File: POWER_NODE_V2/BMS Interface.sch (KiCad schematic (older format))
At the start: 0 parts

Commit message: WIP
making good progress
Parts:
- added J?: CONN_02X07, symbol CONN_02X07
- added J?: CONN_01X02, symbol CONN_01X02
- added Q?: Q_NMOS_GSD, symbol Q_NMOS_GSD
- added R? (x2): 10K / .1W / 1% / SMD 0603, symbol R
- added R?: 100 / .1W / 10% / SMD 0603, symbol R
- added U?: MAX14850AEE+, symbol MAX14850AEE+
- added U?: MAX14932, symbol MAX14932
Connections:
- net BMS_ALERT: now also U?.5 (OUTA2)
- net BMS_COMMS_EN: now also J?.13 (P13)
- net BMS_CONV: now also U?.3 (INA1)
- net BMS_DRDY: now also U?.5 (OUTA2)
- net BMS_FAN: now also R?.2
- net BMS_FAULT: now also U?.4 (OUTA1)
- net BMS_MISO: now also U?.4 (OUTA1)
- net BMS_MOSI: now also U?.2 (INA1)
- net BMS_NCS: now also R?.2, U?.6 (IOA1)
- net BMS_SCK: now also U?.3 (INA2)
- new net: J?.7 (P7), U?.11 (IOB1)
- new net: J?.4 (P4), R?.2, U?.12 (INB2)
- new net: J?.1 (P1), U?.13 (INB1)
- new net: J?.5 (P5), U?.14 (OUTB2)
- new net: J?.3 (P3), U?.15 (OUTB1)
- new net: J?.14 (P14), R?.1, U?.16 (VCCB), U?.16 (VCCB)
- new net: J?.2 (P2), U?.15 (GNDB), U?.9 (GNDB), U?.9 (GNDB)
- new net: J?.8 (P8), U?.11 (INB2)
- new net: J?.10 (P10), U?.12 (INB1)
- new net: J?.9 (P9), U?.14 (OUTB1)
- new net: J?.2 (P2), Q?.3 (D)
- new net: Q?.1 (G), R?.1
- new net +24V: J?.1 (P1)
- new net +3V3: J?.6 (P6), R?.1, U?.1 (VCCA), U?.1 (VCCA)
- new net 1-Wire: J?.12 (P12)
- new net GND: J?.11 (P11), Q?.2 (S), U?.2 (GNDA), U?.8 (GNDA), U?.8 (GNDA)
- no-connect marks 0 -> 4
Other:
- note added: "TODO: Spec suffix for off pin state,\nbypass caps\n"

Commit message: WIP
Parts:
- Q?: value Q_NMOS_GSD -> FDN337N
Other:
- note added: "TODO: Spec suffix for off pin state,\nbypass caps\nflyback diode on fan"
- note removed: "TODO: Spec suffix for off pin state,\nbypass caps\n"
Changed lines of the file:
@@
 $EndComp
 Text Notes 7600 5850 0    197  ~ 0
-TODO: Spec suffix for off pin state,\nbypass caps\n
+TODO: Spec suffix for off pin state,\nbypass caps\nflyback diode on fan
 Wire Wire Line
 	2200 2050 3550 2050
@@
 P 4600 7100
 F 0 "Q?" H 4800 7150 50  0000 L CNN
-F 1 "Q_NMOS_GSD" H 4800 7050 50  0000 L CNN
+F 1 "FDN337N" H 4800 7050 50  0000 L CNN
 F 2 "" H 4800 7200 50  0001 C CNN
 F 3 "" H 4600 7100 50  0001 C CNN

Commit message: more wip
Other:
- note added: "TODO: Spec suffix for off pin state,\nbypass caps\nflyback diode on fan\nFAN Driver: NCV8405ADTRKG"
- note removed: "TODO: Spec suffix for off pin state,\nbypass caps\nflyback diode on fan"
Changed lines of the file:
@@
 $EndComp
 Text Notes 7600 5850 0    197  ~ 0
-TODO: Spec suffix for off pin state,\nbypass caps\nflyback diode on fan
+TODO: Spec suffix for off pin state,\nbypass caps\nflyback diode on fan\nFAN Driver: NCV8405ADTRKG
 Wire Wire Line
 	2200 2050 3550 2050

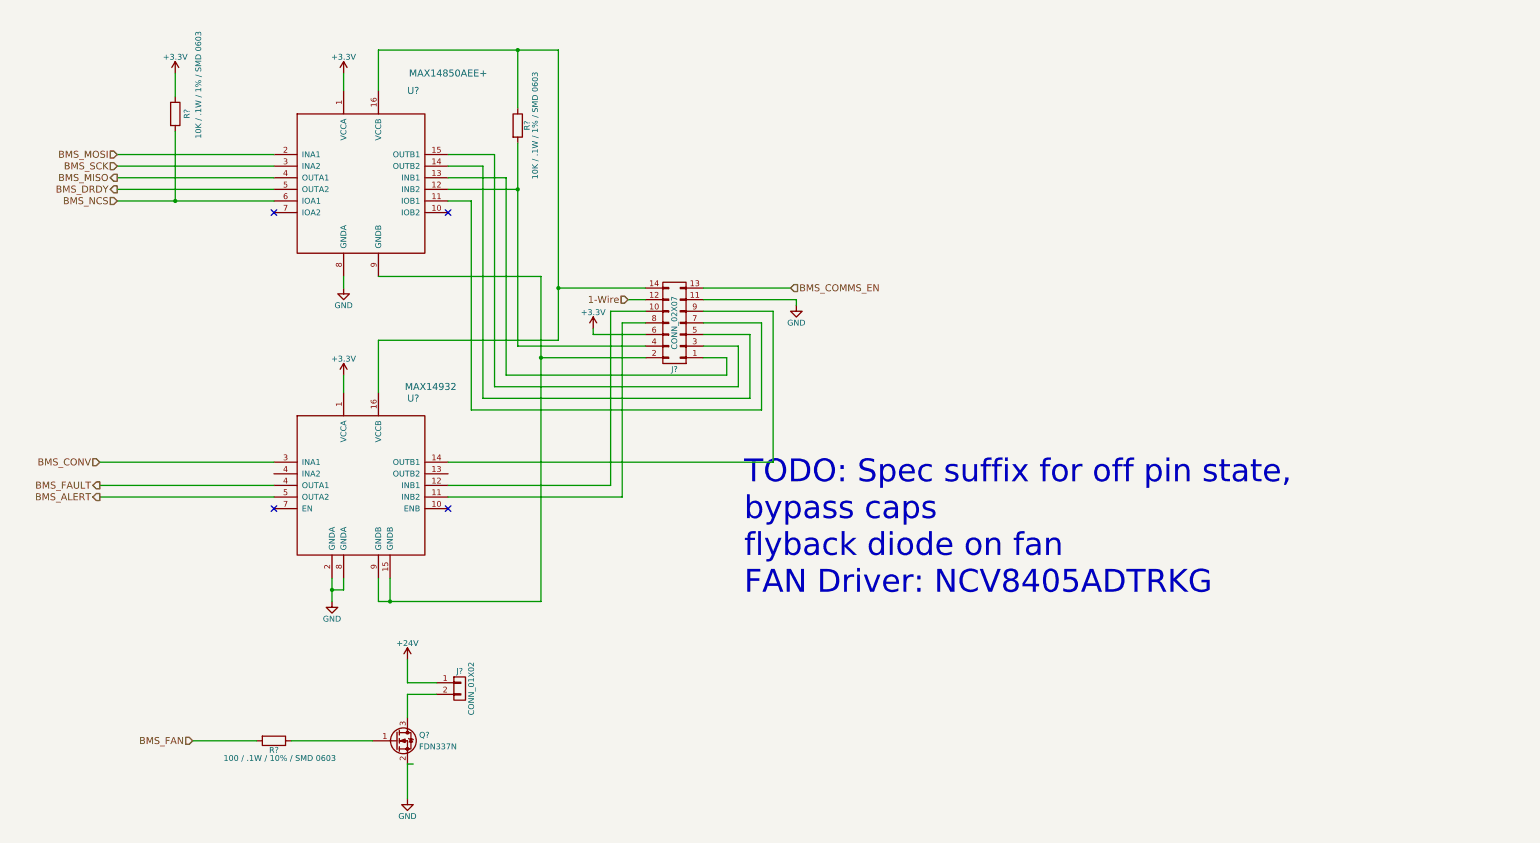
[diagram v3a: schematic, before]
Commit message: Schematic for Power Node V2 mostly done - mostly need connectors
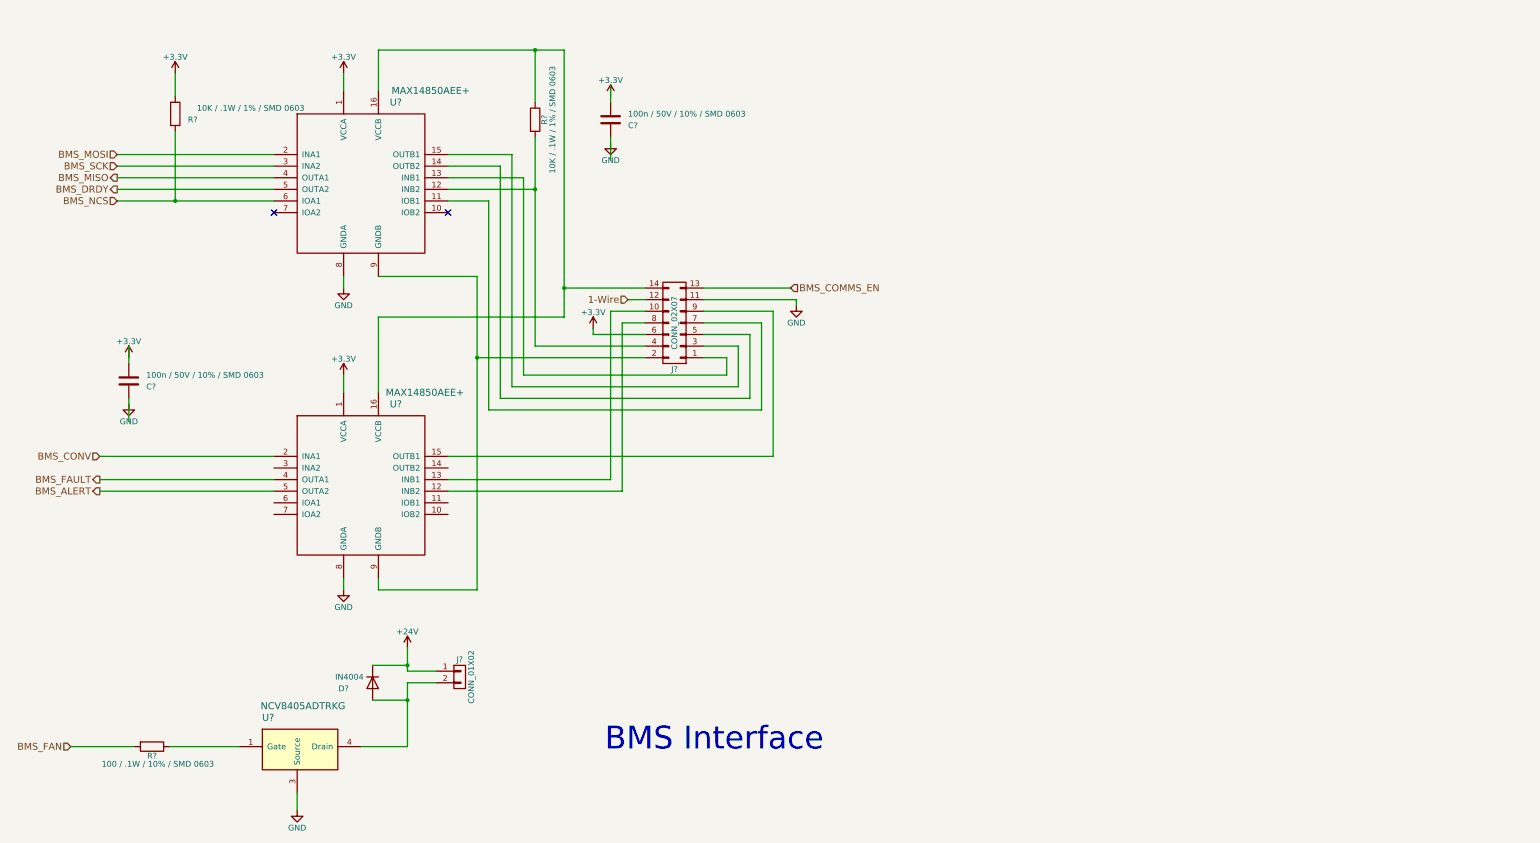
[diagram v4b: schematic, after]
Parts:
- removed Q?: FDN337N, symbol Q_NMOS_GSD
- removed U?: MAX14932, symbol MAX14932
- added C? (x2): 100n / 50V / 10% / SMD 0603, symbol C
- added D?: IN4004, symbol D
- added U?: MAX14850AEE+, symbol MAX14850AEE+
- added U?: NCV8405ADTRKG, symbol NCV8405ADTRKG
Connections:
- wire segments 75 -> 78
- no-connect marks 4 -> 2
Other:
- note added: "BMS Interface"
- note removed: "TODO: Spec suffix for off pin state,\nbypass caps\nflyback diode on fan\nFAN Driver: NCV8405ADTRKG"
- moved on the sheet: J?, R?
